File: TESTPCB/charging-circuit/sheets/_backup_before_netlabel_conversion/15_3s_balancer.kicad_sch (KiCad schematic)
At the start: 32 parts, among them J10 Conn_01x02, J11 Conn_01x04, Q4 BSS84, Q5 AO4892, SW1 TS-1088R-02026, U14 NTC10K/0805/F, U15 BQ76920PW

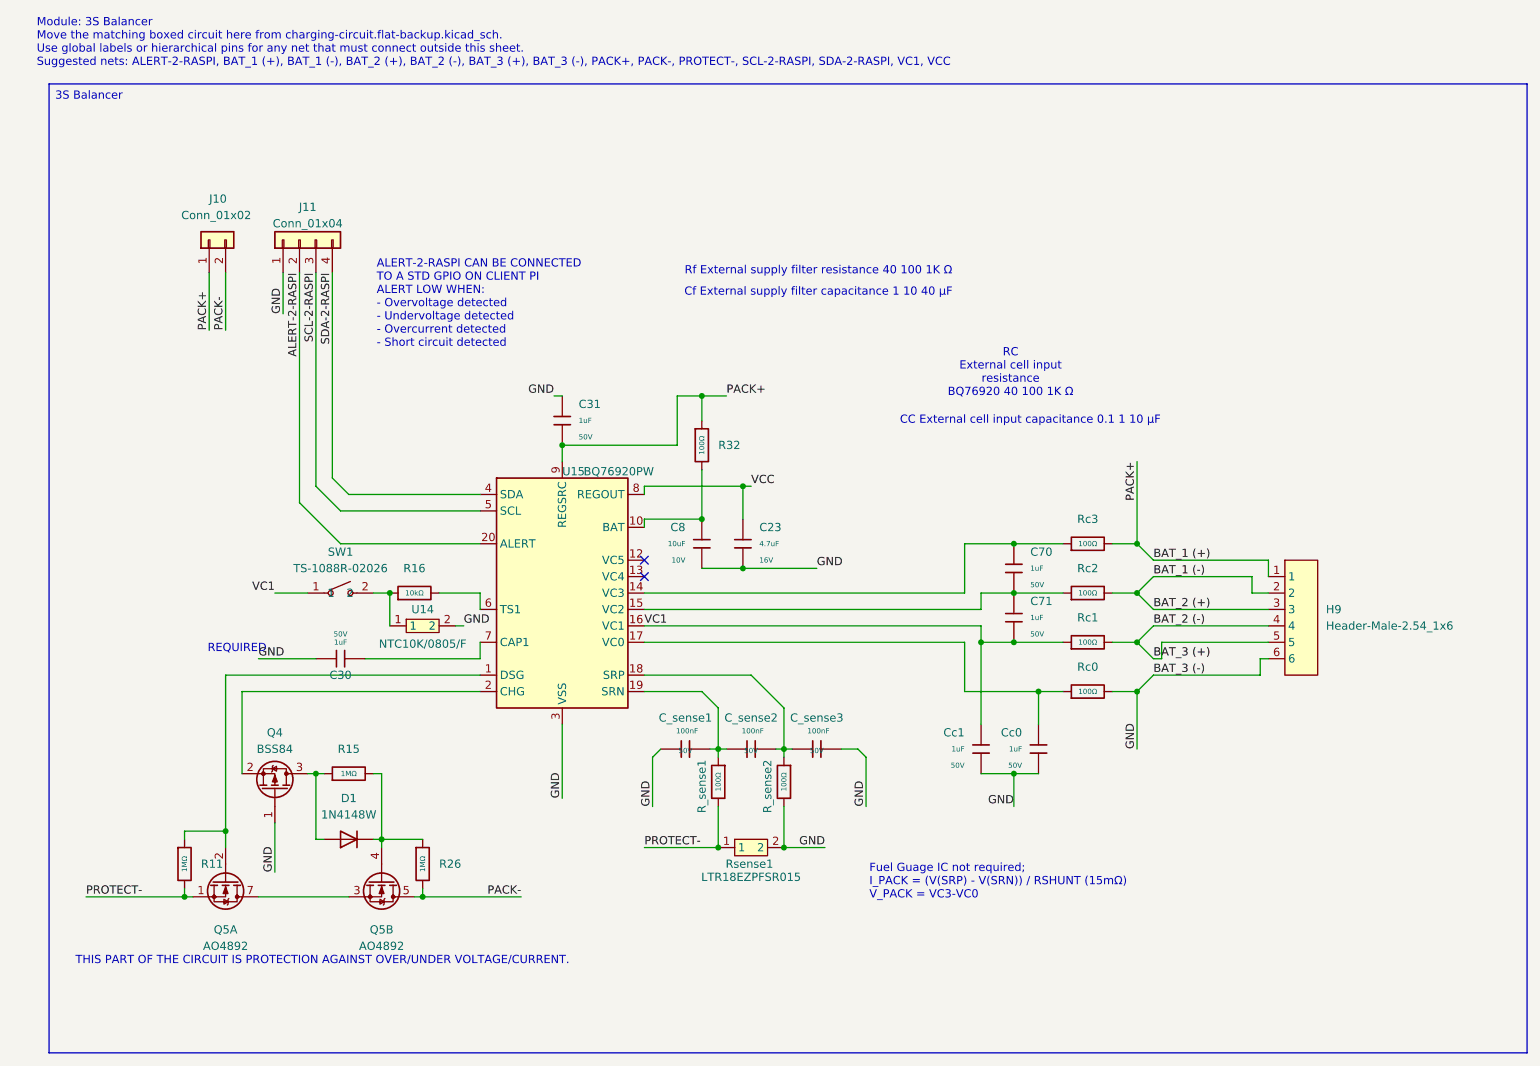
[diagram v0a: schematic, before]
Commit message: Fixed formatting issues, now the hierachal sheets are all labeled as net labels and when we want to expose their pins we will make them into hierchal or global pins
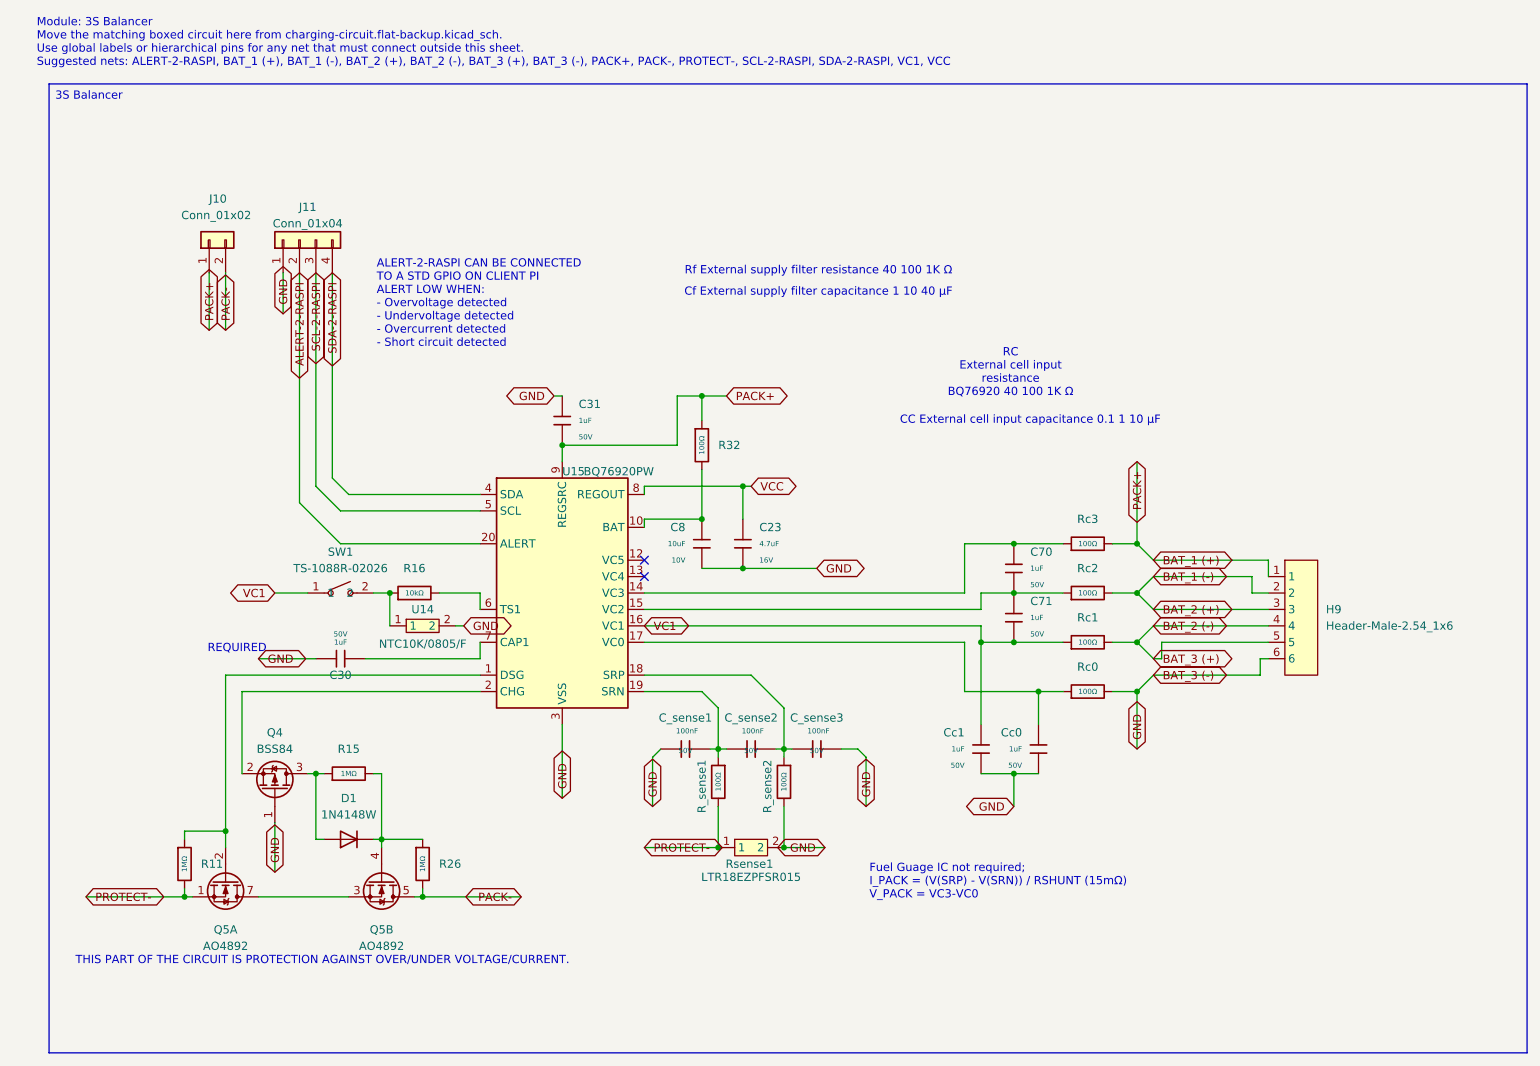
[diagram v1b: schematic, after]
